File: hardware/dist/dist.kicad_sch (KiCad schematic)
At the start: 52 parts, among them J1 PJ301M, J10 Conn_02x08_Odd_Even, J2 PJ301M, J3 PJ301M, J4 PJ301M, J5 PJ301M, J6 PJ301M, J7 PJ301M, J8 PJ301M, J9 Jack-DC, SW1 SW_SPDT, SW2 SW_SPDT, SW3 SW_SPDT, U1 TL072, U2 TL072, U3 TL072, U4 TL072, U5 TL072, U6 TL072, U7 TL072, U8 TL072, U9 TL072

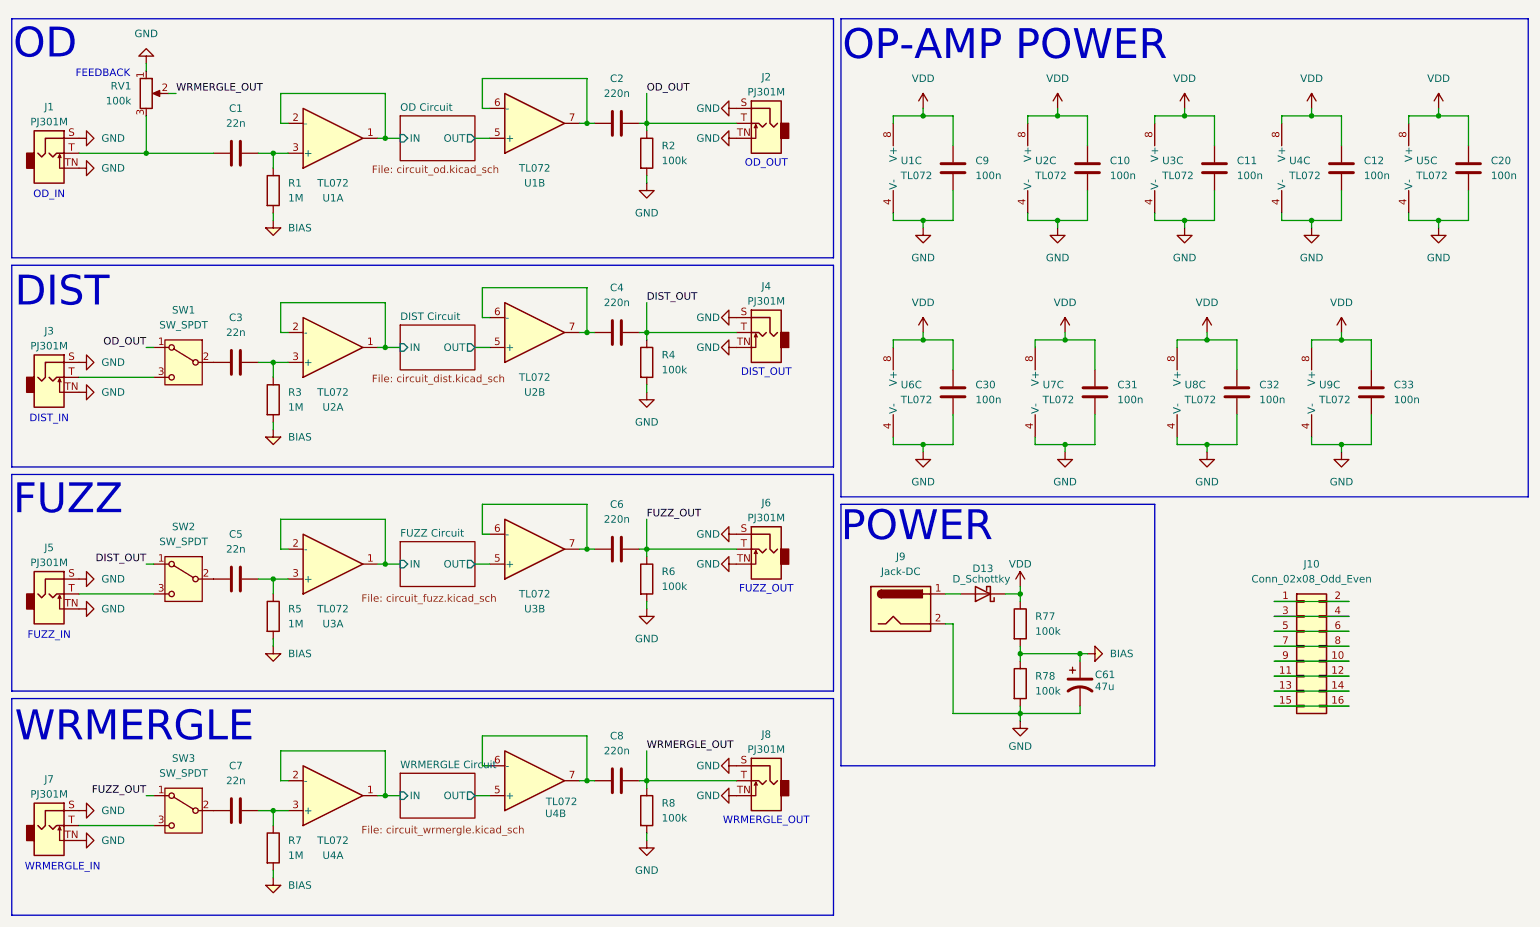
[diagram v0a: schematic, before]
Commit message: bom + kicad fix for dual supply
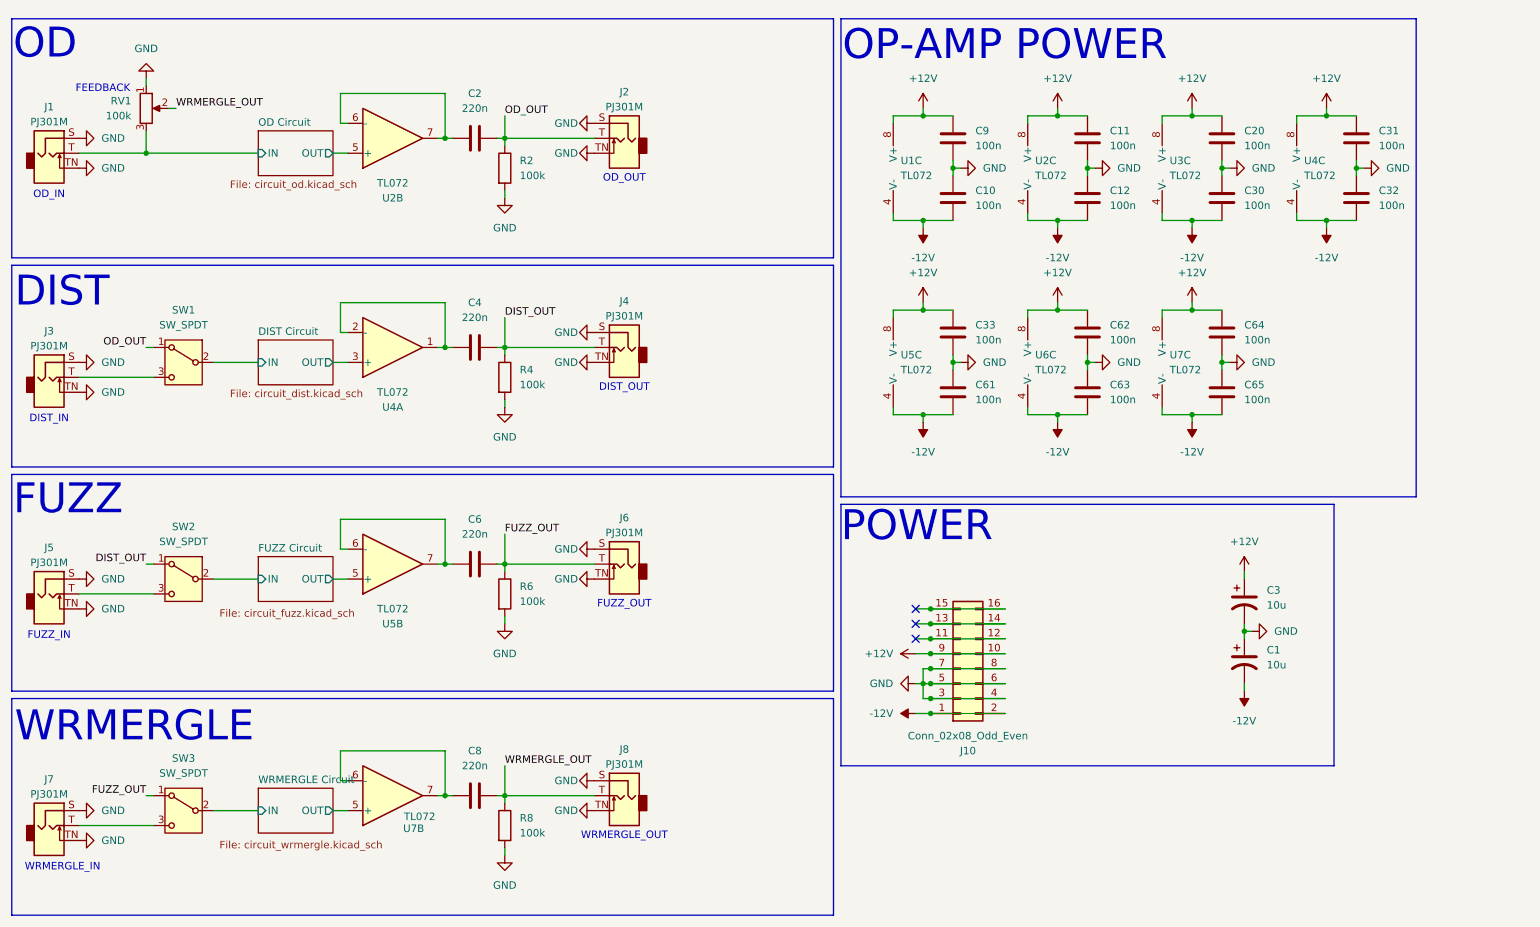
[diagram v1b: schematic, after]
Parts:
- removed C1, C3, C5, C7: 22n, symbol Device:C
- removed C61: 47u, symbol Device:C_Polarized_US
- removed D13: D_Schottky, symbol Device:D_Schottky
- removed J9: Jack-DC, symbol Connector:Jack-DC
- removed R1, R3, R5, R7: 1M, symbol Device:R
- removed R77, R78: 100k, symbol Device:R
- removed unit 1 of U1
- removed unit 1 of U2
- removed unit 1 of U3
- removed unit 1 of U4
- removed U8, U9: TL072, symbol Amplifier_Operational:TL072
- added C1, C3: 10u, Capacitor_THT:CP_Radial_D4.0mm_P1.50mm, symbol Device:C_Polarized_US
- added C61, C62, C63, C64, C65: 100n, Capacitor_SMD:C_0402_1005Metric, symbol Device:C
- C10, C11, C12, C2, C20, C30, C31, C32, C33, C4, C6, C8, C9: footprint (none) -> Capacitor_SMD:C_0402_1005Metric
- J1, J2, J3, J4, J5, J6, J7, J8: footprint (none) -> PJ301M-12:Jack_3.5mm_QingPu_WQP-PJ301M-12_Vertical
- J10: footprint (none) -> Connector_IDC:IDC-Header_2x08_P2.54mm_Vertical
- R2, R4, R6, R8: footprint (none) -> Resistor_SMD:R_0402_1005Metric
- RV1: footprint (none) -> Potentiometer_THT:Potentiometer_Alps_RK09K_Single_Vertical
- SW1, SW2, SW3: footprint (none) -> Connector_PinHeader_2.54mm:PinHeader_1x03_P2.54mm_Vertical
- U1, U2, U3, U4, U5, U6, U7: footprint (none) -> TL072CDT:D8_TEX_STM
- U2: renamed from U1; footprint (none) -> TL072CDT:D8_TEX_STM
- U4: renamed from U2; footprint (none) -> TL072CDT:D8_TEX_STM
- U5: renamed from U3; footprint (none) -> TL072CDT:D8_TEX_STM
- U7: renamed from U4; footprint (none) -> TL072CDT:D8_TEX_STM
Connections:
- net DIST Circuit/IN: now also SW1.2 (B)
- net DIST Circuit/OUT: now also U4.3 (+); no longer U4.5 (+)
- net FUZZ Circuit/IN: now also SW2.2 (B)
- net GND: now also C10.1, C12.1, C30.1, C32.1, J10.3 (Pin_3), J10.4 (Pin_4), J10.5 (Pin_5), J10.6 (Pin_6), J10.7 (Pin_7), J10.8 (Pin_8), C1.1, C3.2, C61.1, C62.2, C63.1, C64.2, C65.1; no longer C10.2, C12.2, C30.2, C32.2, U1.4 (V-), U2.4 (V-), U3.4 (V-), U4.4 (V-), U5.4 (V-), U6.4 (V-), U7.4 (V-)
- net OD Circuit/IN: now also J1.T, RV1.3
- net WRMERGLE Circuit/IN: now also SW3.2 (B)
- net -12V: now reaches J10.1 (Pin_1), J10.2 (Pin_2)
- net -12V: now also C10.2, C12.2, C30.2, C32.2, U1.4 (V-), U2.4 (V-), U3.4 (V-), U4.4 (V-), U5.4 (V-), U6.4 (V-), U7.4 (V-), C1.2, C61.2, C63.2, C65.2
- net +12V: now reaches J10.10 (Pin_10), J10.9 (Pin_9)
- net +12V: now also C11.1, C20.1, C31.1, C33.1, C9.1, U1.8 (V+), U2.8 (V+), U3.8 (V+), U4.8 (V+), U5.8 (V+), U6.8 (V+), U7.8 (V+), C3.1, C62.1, C64.1
- removed net VDD: C10.1, C11.1, C12.1, C20.1, C30.1, C31.1, C32.1, C33.1, C9.1, U1.8 (V+), U2.8 (V+), U3.8 (V+), U4.8 (V+), U5.8 (V+), U6.8 (V+), U7.8 (V+)
- new net: C4.1, U4.1, U4.2 (-)
- no-connect marks 0 -> 3
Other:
- moved on the sheet: C2, C4, C6, C8, C9, J2, J4, J6, J8, R2, R4, R6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

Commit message: finish pcb
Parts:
- C10, C11, C12, C2, C20, C30, C31, C32, C33, C4, C6, C61, C62, C63, C64, C65, C8, C9: footprint Capacitor_SMD:C_0402_1005Metric -> Capacitor_SMD:C_0805_2012Metric_Pad1.18x1.45mm_HandSolder
- R2, R4, R6, R8: footprint Resistor_SMD:R_0402_1005Metric -> Resistor_SMD:R_0805_2012Metric_Pad1.20x1.40mm_HandSolder
- renumbered U5 to U4
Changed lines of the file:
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@@
 			)
 		)
-		(property "Footprint" "Capacitor_SMD:C_0402_1005Metric"
+		(property "Footprint" "Capacitor_SMD:C_0805_2012Metric_Pad1.18x1.45mm_HandSolder"
 			(at 174.9552 38.1 0)
 			(hide yes)
@@
 			)
 		)
-		(property "Footprint" "Capacitor_SMD:C_0402_1005Metric"
+		(property "Footprint" "Capacitor_SMD:C_0805_2012Metric_Pad1.18x1.45mm_HandSolder"
 			(at 220.6752 71.12 0)
 			(hide yes)
@@
 			)
 		)
-		(property "Footprint" "Resistor_SMD:R_0402_1005Metric"
+		(property "Footprint" "Resistor_SMD:R_0805_2012Metric_Pad1.20x1.40mm_HandSolder"
 			(at 96.012 39.37 90)
 			(hide yes)
@@
 			)
 		)
-		(property "Footprint" "Capacitor_SMD:C_0402_1005Metric"
+		(property "Footprint" "Capacitor_SMD:C_0805_2012Metric_Pad1.18x1.45mm_HandSolder"
 			(at 243.5352 48.26 0)
 			(hide yes)
@@
 			)
 		)
-		(property "Footprint" "Capacitor_SMD:C_0402_1005Metric"
+		(property "Footprint" "Capacitor_SMD:C_0805_2012Metric_Pad1.18x1.45mm_HandSolder"
 			(at 197.8152 38.1 0)
 			(hide yes)
@@
 			)
 		)
-		(property "Footprint" "Capacitor_SMD:C_0402_1005Metric"
+		(property "Footprint" "Capacitor_SMD:C_0805_2012Metric_Pad1.18x1.45mm_HandSolder"
 			(at 197.8152 71.12 0)
 			(hide yes)
@@
 			)
 		)
-		(property "Footprint" "Capacitor_SMD:C_0402_1005Metric"
+		(property "Footprint" "Capacitor_SMD:C_0805_2012Metric_Pad1.18x1.45mm_HandSolder"
 			(at 96.52 68.8848 0)
 			(hide yes)
@@
 			)
 		)
-		(property "Footprint" "Capacitor_SMD:C_0402_1005Metric"
+		(property "Footprint" "Capacitor_SMD:C_0805_2012Metric_Pad1.18x1.45mm_HandSolder"
 			(at 96.52 145.0848 0)
 			(hide yes)
@@
 			)
 		)
-		(property "Footprint" "Capacitor_SMD:C_0402_1005Metric"
+		(property "Footprint" "Capacitor_SMD:C_0805_2012Metric_Pad1.18x1.45mm_HandSolder"
 			(at 174.9552 48.26 0)
 			(hide yes)
@@
 			)
 		)
-		(property "Footprint" "Resistor_SMD:R_0402_1005Metric"
+		(property "Footprint" "Resistor_SMD:R_0805_2012Metric_Pad1.20x1.40mm_HandSolder"
 			(at 96.012 111.76 90)
 			(hide yes)
@@
 			)
 		)
-		(property "Footprint" "Resistor_SMD:R_0402_1005Metric"
+		(property "Footprint" "Resistor_SMD:R_0805_2012Metric_Pad1.20x1.40mm_HandSolder"
 			(at 96.012 151.13 90)
 			(hide yes)
@@
 			)
 		)
-		(property "Footprint" "Capacitor_SMD:C_0402_1005Metric"
+		(property "Footprint" "Capacitor_SMD:C_0805_2012Metric_Pad1.18x1.45mm_HandSolder"
 			(at 174.9552 71.12 0)
 			(hide yes)
@@
 			)
 		)
-		(property "Footprint" "Capacitor_SMD:C_0402_1005Metric"
+		(property "Footprint" "Capacitor_SMD:C_0805_2012Metric_Pad1.18x1.45mm_HandSolder"
 			(at 220.6752 48.26 0)
 			(hide yes)
@@
 			)
 		)
-		(property "Footprint" "Capacitor_SMD:C_0402_1005Metric"
+		(property "Footprint" "Capacitor_SMD:C_0805_2012Metric_Pad1.18x1.45mm_HandSolder"
 			(at 174.9552 81.28 0)
 			(hide yes)
@@
 			)
 		)
-		(property "Footprint" "Capacitor_SMD:C_0402_1005Metric"
+		(property "Footprint" "Capacitor_SMD:C_0805_2012Metric_Pad1.18x1.45mm_HandSolder"
 			(at 96.52 33.3248 0)
 			(hide yes)
@@
 			)
 		)
-		(property "Footprint" "Capacitor_SMD:C_0402_1005Metric"
+		(property "Footprint" "Capacitor_SMD:C_0805_2012Metric_Pad1.18x1.45mm_HandSolder"
 			(at 197.8152 81.28 0)
 			(hide yes)
@@
 			)
 		)
-		(property "Footprint" "Capacitor_SMD:C_0402_1005Metric"
+		(property "Footprint" "Capacitor_SMD:C_0805_2012Metric_Pad1.18x1.45mm_HandSolder"
 			(at 96.52 105.7148 0)
 			(hide yes)
@@
 			)
 		)
-		(property "Footprint" "Capacitor_SMD:C_0402_1005Metric"
+		(property "Footprint" "Capacitor_SMD:C_0805_2012Metric_Pad1.18x1.45mm_HandSolder"
 			(at 220.6752 81.28 0)
 			(hide yes)
@@
 			)
 		)
-		(property "Footprint" "Capacitor_SMD:C_0402_1005Metric"
+		(property "Footprint" "Capacitor_SMD:C_0805_2012Metric_Pad1.18x1.45mm_HandSolder"
 			(at 220.6752 38.1 0)
 			(hide yes)
@@
 			)
 		)
-		(property "Footprint" "Capacitor_SMD:C_0402_1005Metric"
+		(property "Footprint" "Capacitor_SMD:C_0805_2012Metric_Pad1.18x1.45mm_HandSolder"
 			(at 197.8152 48.26 0)
 			(hide yes)
@@
 			)
 		)
-		(property "Footprint" "Capacitor_SMD:C_0402_1005Metric"
+		(property "Footprint" "Capacitor_SMD:C_0805_2012Metric_Pad1.18x1.45mm_HandSolder"
 			(at 243.5352 38.1 0)
 			(hide yes)
@@
 		(in_pos_files yes)
 		(dnp no)
-		(property "Reference" "U5"
+		(property "Reference" "U4"
 			(at 78.74 116.84 0)
 			(show_name no)
@@
 			(project "dist"
 				(path "/80db04cd-294a-4ba1-be3a-1807808f6a1c"
-					(reference "U5")
+					(reference "U4")
 					(unit 2)
 				)
@@
 			)
 		)
-		(property "Footprint" "Resistor_SMD:R_0402_1005Metric"
+		(property "Footprint" "Resistor_SMD:R_0805_2012Metric_Pad1.20x1.40mm_HandSolder"
 			(at 96.012 74.93 90)
 			(hide yes)
